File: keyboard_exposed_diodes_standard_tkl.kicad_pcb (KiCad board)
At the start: 2 copper layers, 362 x 177 mm, 317 parts, among them J1 Conn_01x02_Male, J2 USB_C_Receptacle_USB2.0, SW1 Rotary_Encoder_Switch, U1 Pico

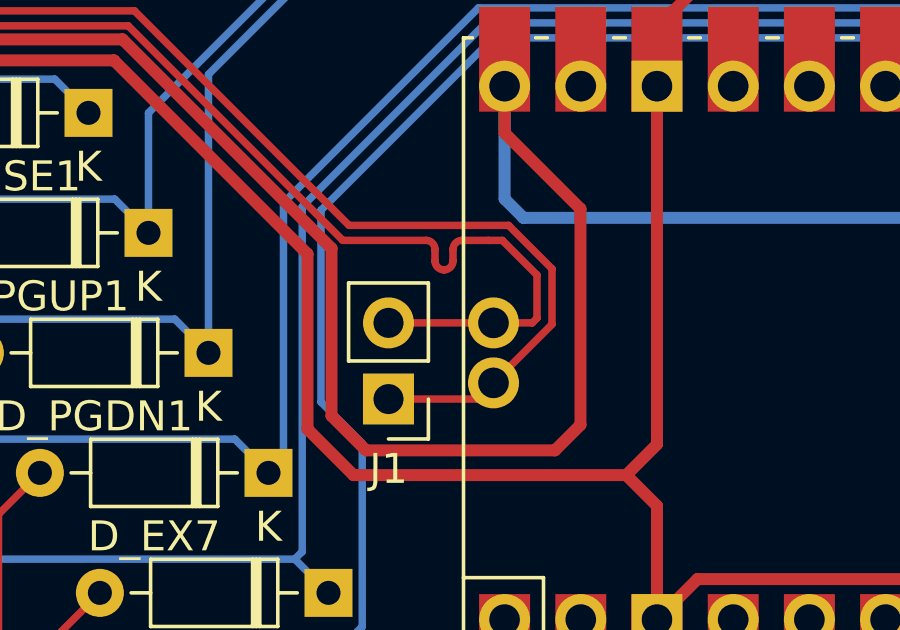
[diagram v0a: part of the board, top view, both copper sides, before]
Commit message: Update pico footprint
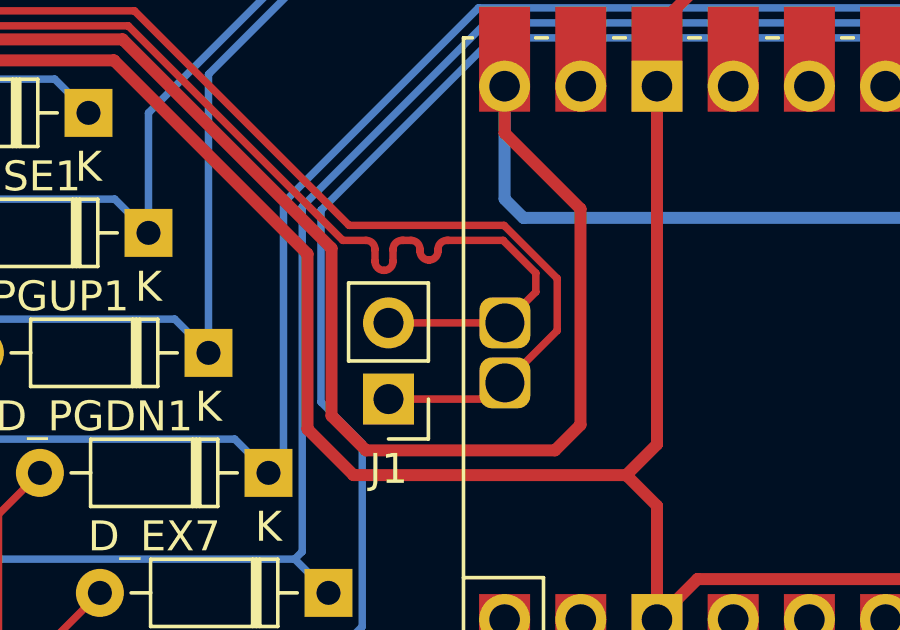
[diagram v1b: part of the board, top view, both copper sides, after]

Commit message: Move hole labels
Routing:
- net COL 13: track 202.3 -> 200.3 mm
- net Net-(D_COMMA1-Pad2): track 145.2 -> 144.2 mm
- net Net-(D_K1-Pad2): track 126.7 -> 125.9 mm

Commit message: Remove step up led. Use gate instead
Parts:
- removed C96: C, Capacitor_SMD:C_0805_2012Metric
- removed D96: D, Diode_THT:D_DO-35_SOD27_P7.62mm_Horizontal
- removed D97: LTST-A683CEGBW, Cherry MX:LTST-A683CEGBW
- added JP1: SolderJumper_2_Open, Jumper:SolderJumper-2_P1.3mm_Open_RoundedPad1.0x1.5mm, B.Cu at (446.0, 189.0)
- added REF_HOLE_16: MountingHole_4.3mm_M4, MountingHole:MountingHole_4.3mm_M4, F.Cu at (114.0, 215.0)
- added REF_HOLE_17: MountingHole_4.3mm_M4, MountingHole:MountingHole_4.3mm_M4, F.Cu at (114.0, 205.0)
- added REF_HOLE_23: MountingHole_4.3mm_M4, MountingHole:MountingHole_4.3mm_M4, F.Cu at (236.2, 221.0)
- added REF_HOLE_24: MountingHole_4.3mm_M4, MountingHole:MountingHole_4.3mm_M4, F.Cu at (322.0, 221.0)
- added REF_HOLE_7: MountingHole_4.3mm_M4, MountingHole:MountingHole_4.3mm_M4, F.Cu at (468.0, 205.0)
- added REF_HOLE_8: MountingHole_4.3mm_M4, MountingHole:MountingHole_4.3mm_M4, F.Cu at (468.0, 215.0)
- added U2: SN74AUP1T34DCK, Package_TO_SOT_SMD:SOT-353_SC-70-5, B.Cu at (443.2, 189.0)
- U1: footprint MCU_RaspberryPi_and_Boards:RPi_Pico_SMD_TH_usb_tp -> MCU_RaspberryPi_and_Boards:RPi_Pico_SMD_TH
- moved J2 2.70 mm to (293.0, 172.0)
- moved REF_HOLE_3 0.09 mm to (275.0, 170.0)
- renumbered REF_HOLE_8 to REF_HOLE_10, REF_HOLE_9 to REF_HOLE_11, REF_HOLE_10 to REF_HOLE_12, REF_HOLE_11 to REF_HOLE_13, REF_HOLE_12 to REF_HOLE_14, REF_HOLE_13 to REF_HOLE_15, REF_HOLE_14 to REF_HOLE_18, REF_HOLE_15 to REF_HOLE_19, REF_HOLE_16 to REF_HOLE_20, REF_HOLE_17 to REF_HOLE_21, REF_HOLE_18 to REF_HOLE_22, REF_HOLE_7 to REF_HOLE_9
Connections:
- U1 pad 24: Net-(D97-Pad2) -> RGB_SIG
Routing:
- net PWR: track 2857.0 -> 2829.0 mm
- net Net-(D97-Pad2): track 21.0 -> 0.00 mm
- net RGB_SIG: track 0.00 -> 20.2 mm
- net Net-(C96-Pad2): track 14.9 -> 0.00 mm
- net Net-(JP1-Pad2): track 53.9 -> 45.5 mm
- net /D-: track 116.5 -> 119.1 mm
- net /D+: track 116.8 -> 119.1 mm
- net GND: track 2956.7 -> 2954.6 mm
- net Net-(D_RBRACK1-Pad2): track 137.5 -> 135.9 mm
- net Net-(D_RIGHT1-Pad2): track 234.2 -> 235.4 mm
- net Net-(D_RCTRL1-Pad2): track 201.3 -> 200.2 mm
- net Net-(D_META1-Pad2): track 217.4 -> 216.4 mm
- net Net-(D_DOWN1-Pad2): track 220.6 -> 221.6 mm
- net Net-(D_5-Pad2): track 72.8 -> 72.2 mm

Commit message: Incude mount holes and stabilizer holes in schematic
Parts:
- renumbered REF_STAB_BKSPC to REF_STAB_BKSPC1, REF_STAB_ENT to REF_STAB_ENT1, REF_STAB_LSHIFT to REF_STAB_LSHIFT1, REF_STAB_RSHIFT to REF_STAB_RSHIFT1, REF_STAB_SPC to REF_STAB_SPC1
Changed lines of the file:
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@@
       (drillshape 0)
       (scaleselection 1)
-      (outputdirectory "I:/anduril.tfotw@gmail.com/Projects/kicad/keyboard_exposed_diodes_standard_tkl/keyboard-diode-gerbers/")
+      (outputdirectory "gerber/")
     )
   )
@@
     (tags "Cherry MX key stabilizer 2u 2.25u 2.5u 2.75u")
     (attr exclude_from_pos_files exclude_from_bom)
-    (fp_text reference "REF_STAB_LSHIFT" (at 0 -3) (layer "F.SilkS")
+    (fp_text reference "REF_STAB_LSHIFT1" (at 0 -3) (layer "F.SilkS")
       (effects (font (size 1 1) (thickness 0.15)))
     )
@@
       (effects (font (size 1 1) (thickness 0.15)))
     )
-    (fp_text user "REF**" (at 63.10125 -0.275) (layer "F.Fab")
+    (fp_text user "REF**" (at -0.10125 -4.225) (layer "F.Fab")
       (effects (font (size 1 1) (thickness 0.15)))
     )
@@
     (tags "Cherry MX key stabilizer 2u 2.25u 2.5u 2.75u")
     (attr exclude_from_pos_files exclude_from_bom)
-    (fp_text reference "REF_STAB_RSHIFT" (at 0 -3) (layer "F.SilkS")
+    (fp_text reference "REF_STAB_RSHIFT1" (at 0 -3) (layer "F.SilkS")
       (effects (font (size 1 1) (thickness 0.15)))
     )
@@
       (effects (font (size 1 1) (thickness 0.15)))
     )
-    (fp_text user "REF**" (at 63.10125 -0.275) (layer "F.Fab")
+    (fp_text user "REF**" (at 0.02375 -4.475) (layer "F.Fab")
       (effects (font (size 1 1) (thickness 0.15)))
     )
@@
     (tags "Cherry MX key stabilizer 2u 2.25u 2.5u 2.75u")
     (attr exclude_from_pos_files exclude_from_bom)
-    (fp_text reference "REF_STAB_ENT" (at 0 -3) (layer "F.SilkS")
+    (fp_text reference "REF_STAB_ENT1" (at 0 -3) (layer "F.SilkS")
       (effects (font (size 1 1) (thickness 0.15)))
     )
@@
       (effects (font (size 1 1) (thickness 0.15)))
     )
-    (fp_text user "REF**" (at 63.10125 -0.275) (layer "F.Fab")
+    (fp_text user "REF**" (at 0.01125 -4.425) (layer "F.Fab")
       (effects (font (size 1 1) (thickness 0.15)))
     )
@@
     (tags "Cherry MX key stabilizer 2u 2.25u 2.5u 2.75u")
     (attr exclude_from_pos_files exclude_from_bom)
-    (fp_text reference "REF_STAB_BKSPC" (at 0 -3) (layer "F.SilkS")
+    (fp_text reference "REF_STAB_BKSPC1" (at 0 -3) (layer "F.SilkS")
       (effects (font (size 1 1) (thickness 0.15)))
     )
@@
       (effects (font (size 1 1) (thickness 0.15)))
     )
-    (fp_text user "REF**" (at 63.10125 -0.275) (layer "F.Fab")
+    (fp_text user "REF**" (at -0.12 -4.575) (layer "F.Fab")
       (effects (font (size 1 1) (thickness 0.15)))
     )
@@
       (effects (font (size 1 1) (thickness 0.15)))
     )
-    (fp_text user "REF**" (at 63.10125 -0.275) (layer "F.Fab")
+    (fp_text user "REF**" (at 0.01125 -4.275) (layer "F.Fab")
       (effects (font (size 1 1) (thickness 0.15)))
     )
@@
     (tags "Cherry MX key stabilizer 2u 2.25u 2.5u 2.75u")
     (attr exclude_from_pos_files exclude_from_bom)
-    (fp_text reference "REF_STAB_SPC" (at 0 -3) (layer "F.SilkS")
+    (fp_text reference "REF_STAB_SPC1" (at 0 -3) (layer "F.SilkS")
       (effects (font (size 1 1) (thickness 0.15)))
     )
